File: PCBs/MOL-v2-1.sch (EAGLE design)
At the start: 27 parts, among them IC1 ULN2803, IC2 ULN2803, J1 SERVO1, J10 JOY1, J11 JOY2, J2 SERVO2, J3 STRIPS, J4 ACTUATORS, J5 POWER-5V, J6 AN-IN-1, J7 AN-IN-2, J8 AN-IN-3, J9 AN-IN-4, SW1 500SSP1S2M2QEA

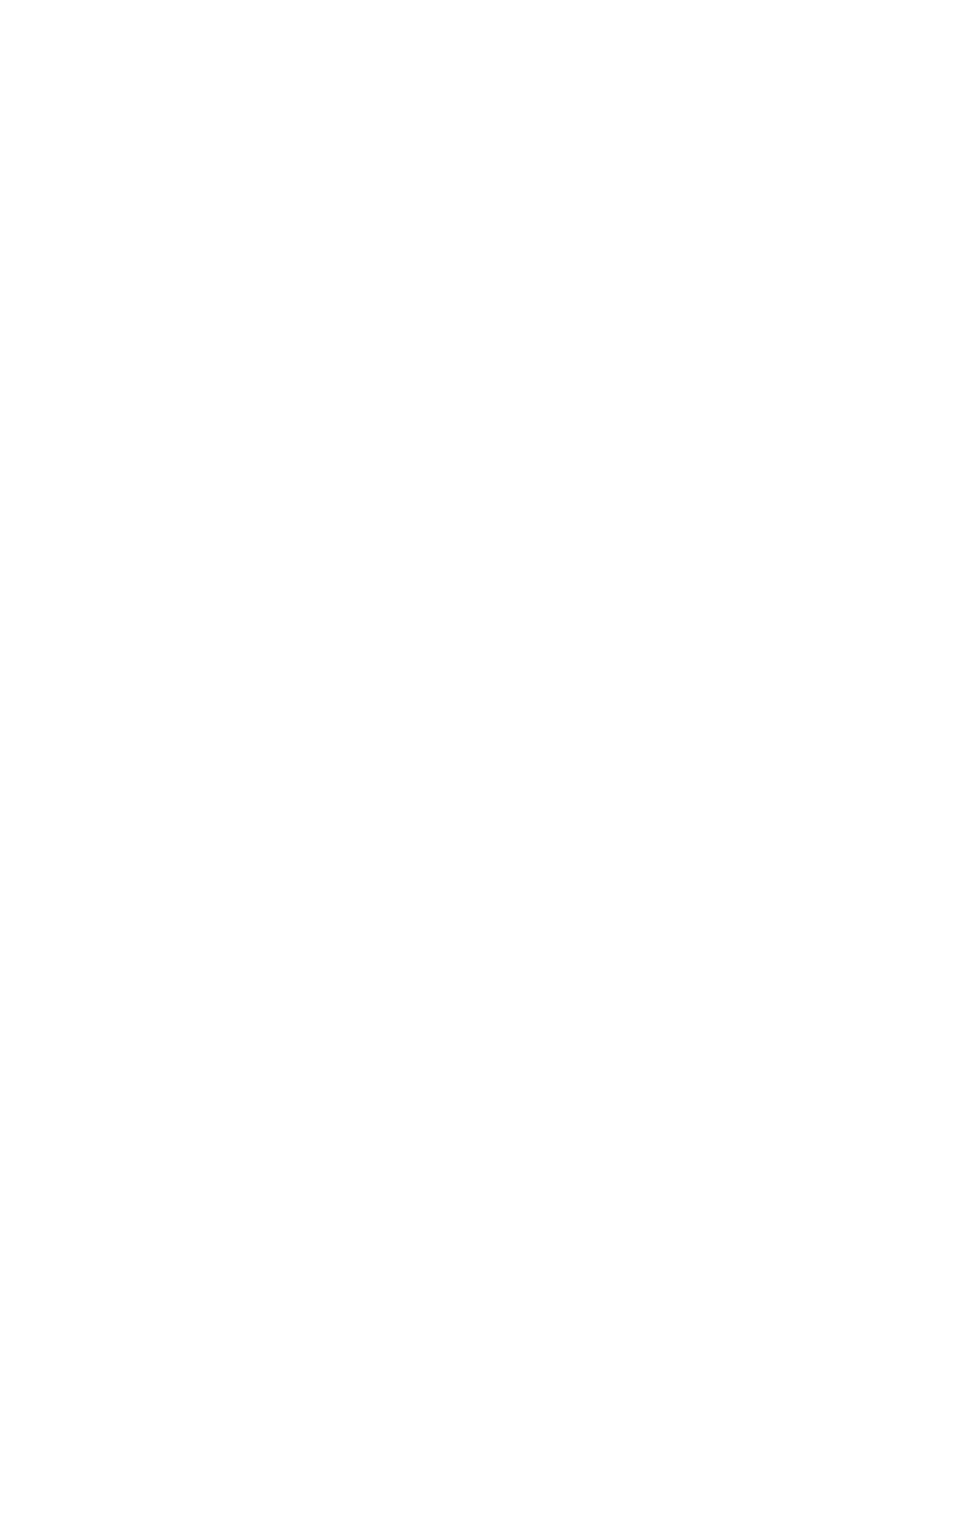
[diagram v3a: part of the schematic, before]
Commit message: mol library
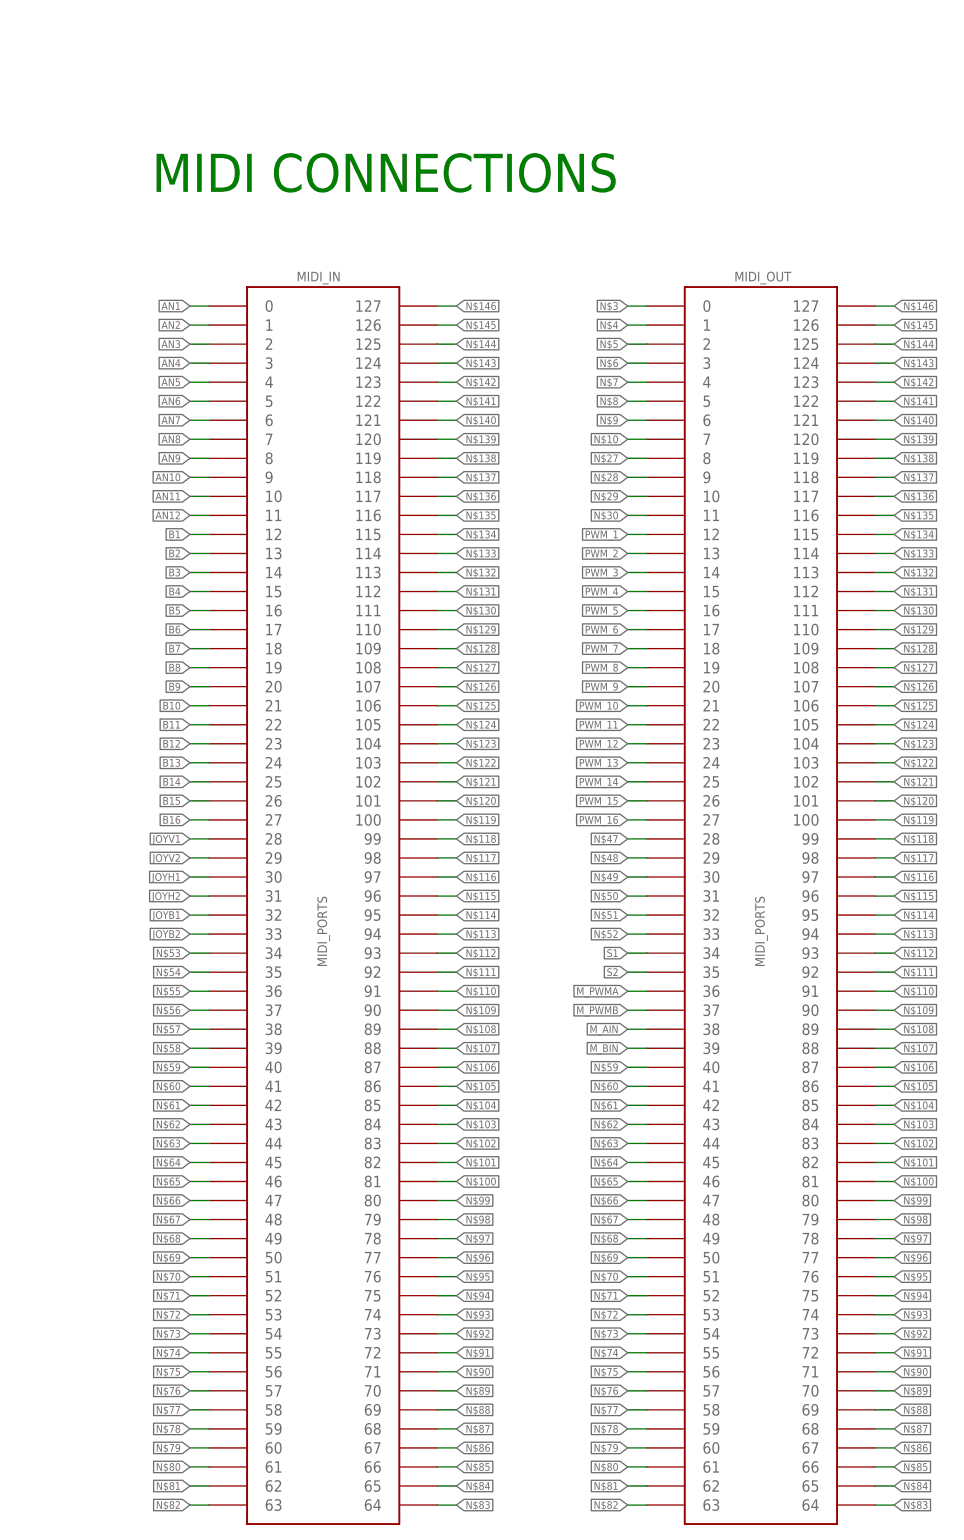
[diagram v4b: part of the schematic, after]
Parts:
- added MIDI_IN, MIDI_OUT: MIDI_PORTS, CMU-ArtFab:MIDI_PORTS
- KNOB1, KNOB2, KNOB3, KNOB4: device Daniel:TRIM -> CMU-ArtFab:TRIM
- renumbered U$1 to TEENSY
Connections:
- new net N$10: MIDI_OUT.7
- new net N$100: MIDI_IN.81, MIDI_OUT.81
- new net N$101: MIDI_IN.82, MIDI_OUT.82
- new net N$102: MIDI_IN.83, MIDI_OUT.83
- new net N$103: MIDI_IN.84, MIDI_OUT.84
- new net N$104: MIDI_IN.85, MIDI_OUT.85
- new net N$105: MIDI_IN.86, MIDI_OUT.86
- new net N$106: MIDI_IN.87, MIDI_OUT.87
- new net N$107: MIDI_IN.88, MIDI_OUT.88
- new net N$108: MIDI_IN.89, MIDI_OUT.89
- new net N$109: MIDI_IN.90, MIDI_OUT.90
- new net N$110: MIDI_IN.91, MIDI_OUT.91
- new net N$111: MIDI_IN.92, MIDI_OUT.92
- new net N$112: MIDI_IN.93, MIDI_OUT.93
- new net N$113: MIDI_IN.94, MIDI_OUT.94
- new net N$114: MIDI_IN.95, MIDI_OUT.95
- new net N$115: MIDI_IN.96, MIDI_OUT.96
- new net N$116: MIDI_IN.97, MIDI_OUT.97
- new net N$117: MIDI_IN.98, MIDI_OUT.98
- new net N$118: MIDI_IN.99, MIDI_OUT.99
- new net N$119: MIDI_IN.100, MIDI_OUT.100
- new net N$120: MIDI_IN.101, MIDI_OUT.101
- new net N$121: MIDI_IN.102, MIDI_OUT.102
- new net N$122: MIDI_IN.103, MIDI_OUT.103
- new net N$123: MIDI_IN.104, MIDI_OUT.104
- new net N$124: MIDI_IN.105, MIDI_OUT.105
- new net N$125: MIDI_IN.106, MIDI_OUT.106
- new net N$126: MIDI_IN.107, MIDI_OUT.107
- new net N$127: MIDI_IN.108, MIDI_OUT.108
- new net N$128: MIDI_IN.109, MIDI_OUT.109
- new net N$129: MIDI_IN.110, MIDI_OUT.110
- new net N$130: MIDI_IN.111, MIDI_OUT.111
- new net N$131: MIDI_IN.112, MIDI_OUT.112
- new net N$132: MIDI_IN.113, MIDI_OUT.113
- new net N$133: MIDI_IN.114, MIDI_OUT.114
- new net N$134: MIDI_IN.115, MIDI_OUT.115
- new net N$135: MIDI_IN.116, MIDI_OUT.116
- new net N$136: MIDI_IN.117, MIDI_OUT.117
- new net N$137: MIDI_IN.118, MIDI_OUT.118
- new net N$138: MIDI_IN.119, MIDI_OUT.119
- new net N$139: MIDI_IN.120, MIDI_OUT.120
- new net N$140: MIDI_IN.121, MIDI_OUT.121
- new net N$141: MIDI_IN.122, MIDI_OUT.122
- new net N$142: MIDI_IN.123, MIDI_OUT.123
- new net N$143: MIDI_IN.124, MIDI_OUT.124
- new net N$144: MIDI_IN.125, MIDI_OUT.125
- new net N$145: MIDI_IN.126, MIDI_OUT.126
- new net N$146: MIDI_IN.127, MIDI_OUT.127
- new net N$27: MIDI_OUT.8
- new net N$28: MIDI_OUT.9
- new net N$29: MIDI_OUT.10
- new net N$3: MIDI_OUT.0
- new net N$30: MIDI_OUT.11
- new net N$4: MIDI_OUT.1
- new net N$47: MIDI_OUT.28
- new net N$48: MIDI_OUT.29
- new net N$49: MIDI_OUT.30
- new net N$5: MIDI_OUT.2
- new net N$50: MIDI_OUT.31
- new net N$51: MIDI_OUT.32
- new net N$52: MIDI_OUT.33
- new net N$53: MIDI_IN.34
- new net N$54: MIDI_IN.35
- new net N$55: MIDI_IN.36
- new net N$56: MIDI_IN.37
- new net N$57: MIDI_IN.38
- new net N$58: MIDI_IN.39
- new net N$59: MIDI_IN.40, MIDI_OUT.40
- new net N$6: MIDI_OUT.3
- new net N$60: MIDI_IN.41, MIDI_OUT.41
- new net N$61: MIDI_IN.42, MIDI_OUT.42
- new net N$62: MIDI_IN.43, MIDI_OUT.43
- new net N$63: MIDI_IN.44, MIDI_OUT.44
- new net N$64: MIDI_IN.45, MIDI_OUT.45
- new net N$65: MIDI_IN.46, MIDI_OUT.46
- new net N$66: MIDI_IN.47, MIDI_OUT.47
- new net N$67: MIDI_IN.48, MIDI_OUT.48
- new net N$68: MIDI_IN.49, MIDI_OUT.49
- new net N$69: MIDI_IN.50, MIDI_OUT.50
- new net N$7: MIDI_OUT.4
- new net N$70: MIDI_IN.51, MIDI_OUT.51
- new net N$71: MIDI_IN.52, MIDI_OUT.52
- new net N$72: MIDI_IN.53, MIDI_OUT.53
- new net N$73: MIDI_IN.54, MIDI_OUT.54
- new net N$74: MIDI_IN.55, MIDI_OUT.55
- new net N$75: MIDI_IN.56, MIDI_OUT.56
- new net N$76: MIDI_IN.57, MIDI_OUT.57
- new net N$77: MIDI_IN.58, MIDI_OUT.58
- new net N$78: MIDI_IN.59, MIDI_OUT.59
- new net N$79: MIDI_IN.60, MIDI_OUT.60
- new net N$8: MIDI_OUT.5
- new net N$80: MIDI_IN.61, MIDI_OUT.61
- new net N$81: MIDI_IN.62, MIDI_OUT.62
- new net N$82: MIDI_IN.63, MIDI_OUT.63
- new net N$83: MIDI_IN.64, MIDI_OUT.64
- new net N$84: MIDI_IN.65, MIDI_OUT.65
- new net N$85: MIDI_IN.66, MIDI_OUT.66
- new net N$86: MIDI_IN.67, MIDI_OUT.67
- new net N$87: MIDI_IN.68, MIDI_OUT.68
- new net N$88: MIDI_IN.69, MIDI_OUT.69
- new net N$89: MIDI_IN.70, MIDI_OUT.70
- new net N$9: MIDI_OUT.6
- new net N$90: MIDI_IN.71, MIDI_OUT.71
- new net N$91: MIDI_IN.72, MIDI_OUT.72
- new net N$92: MIDI_IN.73, MIDI_OUT.73
- new net N$93: MIDI_IN.74, MIDI_OUT.74
- new net N$94: MIDI_IN.75, MIDI_OUT.75
- new net N$95: MIDI_IN.76, MIDI_OUT.76
- new net N$96: MIDI_IN.77, MIDI_OUT.77
- new net N$97: MIDI_IN.78, MIDI_OUT.78
- new net N$98: MIDI_IN.79, MIDI_OUT.79
- new net N$99: MIDI_IN.80, MIDI_OUT.80
- net AN1: now also MIDI_IN.0
- net AN10: now also MIDI_IN.9
- net AN11: now also MIDI_IN.10
- net AN12: now also MIDI_IN.11
- net AN2: now also MIDI_IN.1
- net AN3: now also MIDI_IN.2
- net AN4: now also MIDI_IN.3
- net AN5: now also MIDI_IN.4
- net AN6: now also MIDI_IN.5
- net AN7: now also MIDI_IN.6
- net AN8: now also MIDI_IN.7
- net AN9: now also MIDI_IN.8
- net B1: now also MIDI_IN.12
- net B10: now also MIDI_IN.21
- net B11: now also MIDI_IN.22
- net B12: now also MIDI_IN.23
- net B13: now also MIDI_IN.24
- net B14: now also MIDI_IN.25
- net B15: now also MIDI_IN.26
- net B16: now also MIDI_IN.27
- net B2: now also MIDI_IN.13
- net B3: now also MIDI_IN.14
- net B4: now also MIDI_IN.15
- net B5: now also MIDI_IN.16
- net B6: now also MIDI_IN.17
- net B7: now also MIDI_IN.18
- net B8: now also MIDI_IN.19
- net B9: now also MIDI_IN.20
- net JOYB1: now also MIDI_IN.32
- net JOYB2: now also MIDI_IN.33
- net JOYH1: now also MIDI_IN.30
- net JOYH2: now also MIDI_IN.31
- net JOYV1: now also MIDI_IN.28
- net JOYV2: now also MIDI_IN.29
- net M_AIN: now also MIDI_OUT.38
- net M_BIN: now also MIDI_OUT.39
- net M_PWMA: now also MIDI_OUT.36
- net M_PWMB: now also MIDI_OUT.37
- net PWM_1: now also MIDI_OUT.12
- net PWM_10: now also MIDI_OUT.21
- net PWM_11: now also MIDI_OUT.22
- net PWM_12: now also MIDI_OUT.23
- net PWM_13: now also MIDI_OUT.24
- net PWM_14: now also MIDI_OUT.25
- net PWM_15: now also MIDI_OUT.26
- net PWM_16: now also MIDI_OUT.27
- net PWM_2: now also MIDI_OUT.13
- net PWM_3: now also MIDI_OUT.14
- net PWM_4: now also MIDI_OUT.15
- net PWM_5: now also MIDI_OUT.16
- net PWM_6: now also MIDI_OUT.17
- net PWM_7: now also MIDI_OUT.18
- net PWM_8: now also MIDI_OUT.19
- net PWM_9: now also MIDI_OUT.20
- net S1: now also MIDI_OUT.34
- net S2: now also MIDI_OUT.35
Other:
- note added: "MIDI CONNECTIONS"
